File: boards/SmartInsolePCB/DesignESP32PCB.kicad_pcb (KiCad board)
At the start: 2 copper layers, 54.2 x 81.5 mm, 60 parts, among them J1 PJS008U-3000-0, J10 Conn_01x02_Pin, J11 Conn_01x02_Pin, J12 Conn_01x02_Pin, J13 Conn_01x05_Socket, J2 Conn_01x02_Pin, J3 Conn_01x02_Pin, J4 Conn_01x02_Pin, J5 Conn_01x02_Pin, J6 Conn_01x02_Pin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

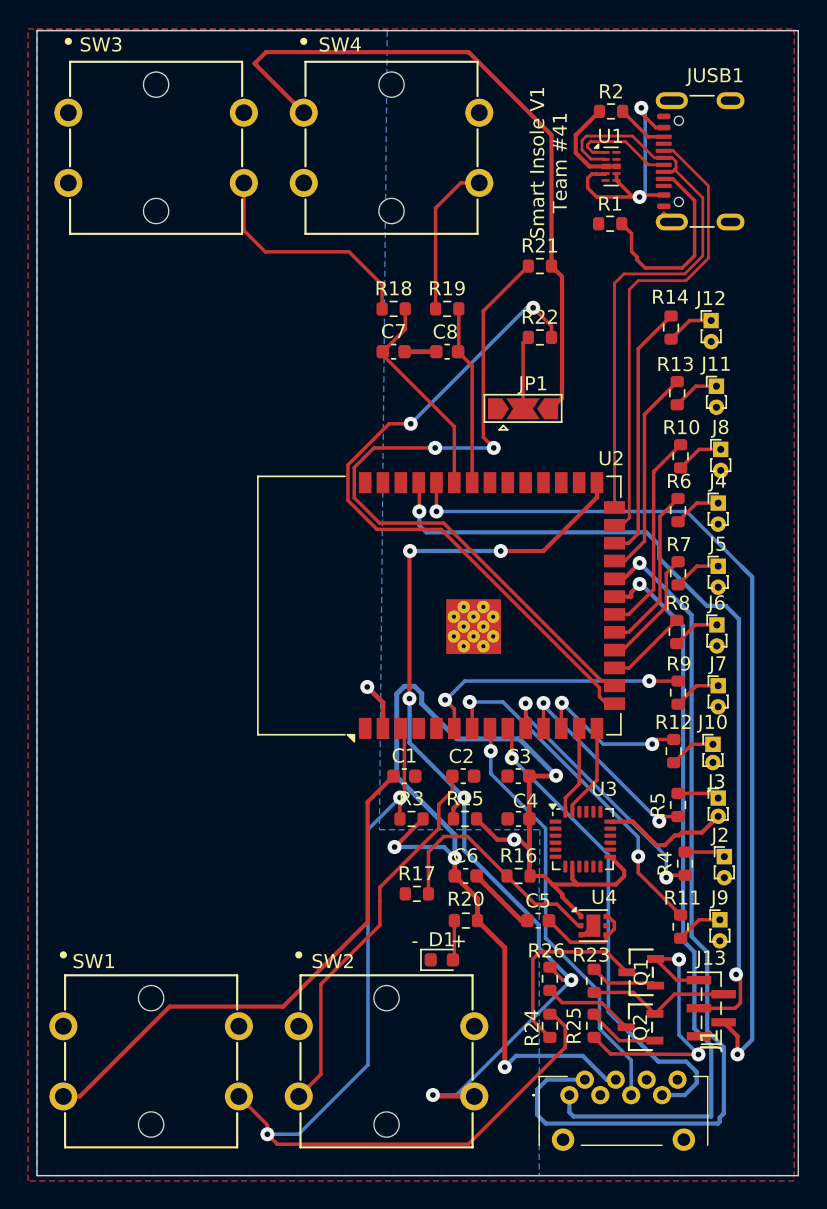
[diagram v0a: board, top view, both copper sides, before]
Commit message: routed all connections
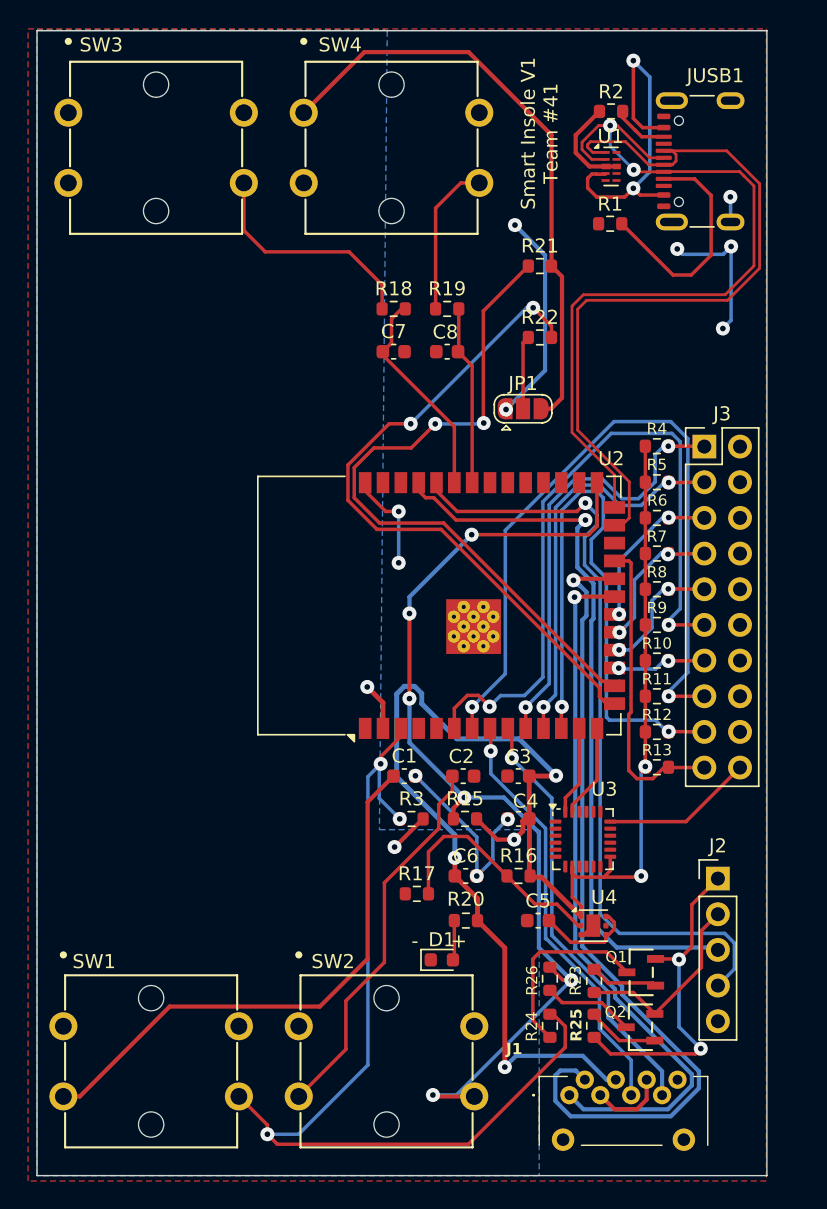
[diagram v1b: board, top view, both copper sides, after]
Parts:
- removed J10, J11, J12, J4, J5, J6, J7, J8, J9: Conn_01x02_Pin, Connector_PinHeader_1.00mm:PinHeader_1x02_P1.00mm_Vertical
- removed J13: Conn_01x05_Socket, Connector_PinHeader_1.00mm:PinHeader_1x05_P1.00mm_Vertical_SMD_Pin1Left
- removed R14: 1k, Resistor_SMD:R_0603_1608Metric
- J2: value Conn_01x02_Pin -> Conn_01x05_Socket; footprint Connector_PinHeader_1.00mm:PinHeader_1x02_P1.00mm_Vertical -> Connector_PinHeader_2.54mm:PinHeader_1x05_P2.54mm_Vertical
- J3: value Conn_01x02_Pin -> Conn_02x10_Odd_Even; footprint Connector_PinHeader_1.00mm:PinHeader_1x02_P1.00mm_Vertical -> Connector_PinHeader_2.54mm:PinHeader_2x10_P2.54mm_Vertical
- JP1: footprint Jumper:SolderJumper-3_P2.0mm_Open_TrianglePad1.0x1.5mm -> Jumper:SolderJumper-3_P1.3mm_Open_RoundedPad1.0x1.5mm
- moved R4 29.8 mm to (135.3, 73.8), turned to 180 degrees
- moved R13 26.7 mm to (135.3, 96.6), turned to 180 degrees
- moved J3 25.1 mm to (138.7, 73.8)
- moved R5 23.0 mm to (135.3, 76.4), turned to 180 degrees
- moved R11 16.5 mm to (135.3, 91.6), turned to 180 degrees
- moved R10 14.6 mm to (135.3, 89.1), turned to 180 degrees
- moved R9 5.05 mm to (135.3, 86.5), turned to 180 degrees
- moved R8 3.35 mm to (135.3, 84.0), turned to 180 degrees
- moved R7 2.06 mm to (135.3, 81.4), turned to 180 degrees
- moved R12 1.82 mm to (135.3, 94.1), turned to 180 degrees
- moved J2 1.63 mm to (139.7, 104.6)
- moved R6 1.61 mm to (135.3, 78.9), turned to 180 degrees
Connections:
- J2 pad 1: Net-(J2-Pin_1) -> /RTS
- J2 pad 2: GND -> /DTR
- J3 pad 1: Net-(J3-Pin_1) -> /GPIO1
- R10 pad 2: Net-(J8-Pin_1) -> /3V3
- R11 pad 2: Net-(J9-Pin_1) -> /3V3
- R12 pad 2: Net-(J10-Pin_1) -> /3V3
- R13 pad 2: Net-(J11-Pin_1) -> /3V3
- R4 pad 2: Net-(J2-Pin_1) -> /3V3
- R5 pad 2: Net-(J3-Pin_1) -> /3V3
- R6 pad 2: Net-(J4-Pin_1) -> /3V3
- R7 pad 2: Net-(J5-Pin_1) -> /3V3
- R8 pad 2: Net-(J6-Pin_1) -> /3V3
- R9 pad 2: Net-(J7-Pin_1) -> /3V3
- U2 pad 17: /GPIO7 -> /GPIO11
- U2 pad 18: /GPIO6 -> /GPIO7
- U2 pad 19: /GPIO3 -> /GPIO6
- U2 pad 20: /GPIO11 -> /GPIO3
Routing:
- net GND: track 25.5 -> 73.3 mm, vias 0 -> 11
- net /GPIO21: track 11.2 -> 43.1 mm
- net /GPIO8: track 19.8 -> 49.9 mm
- net /GPIO12: track 25.2 -> 53.3 mm
- net /3V3: track 140.9 -> 163.7 mm, vias 6 -> 8
- net /GPIO47: track 18.4 -> 0.00 mm
- net /USB_N: track 41.7 -> 58.1 mm, vias 0 -> 2
- net /USB_P: track 41.3 -> 55.9 mm
- net /GPIO2: track 15.1 -> 28.7 mm
- net /GPIO1: track 19.7 -> 31.9 mm
- net /GPIO11: track 14.6 -> 6.20 mm, vias 0 -> 2
- net /RX: track 64.0 -> 56.4 mm, vias 2 -> 1
- net /TX: track 60.2 -> 52.7 mm, vias 2 -> 1
- net /GPIO10: track 15.0 -> 22.4 mm
- net /5VUSB: track 19.4 -> 24.9 mm
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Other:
- board size 54.2 x 81.5 mm -> 52 x 81.5 mm
